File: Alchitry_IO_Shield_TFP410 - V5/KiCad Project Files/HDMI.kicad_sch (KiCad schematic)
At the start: 19 parts, among them J1 HDMI_A_1.4, U2 TFP410

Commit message: started new shield
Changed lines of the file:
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@@
-(kicad_sch (version 20200714) (host eeschema "(5.99.0-2416-g010316457)")
-  (page 1 3)
+(kicad_sch (version 20200714) (host eeschema "(5.99.0-2671-gfc0a358ba)")
+  (page 2 3)
   (paper "A4")
-  (junction (at 95.25 67.945) (diameter 0) (color 0 0 0 0))
-  (junction (at 95.25 69.215) (diameter 0) (color 0 0 0 0))
-  (junction (at 95.25 70.485) (diameter 0) (color 0 0 0 0))
-  (junction (at 95.25 88.265) (diameter 0) (color 0 0 0 0))
-  (junction (at 95.25 89.535) (diameter 0) (color 0 0 0 0))
-  (junction (at 95.25 90.805) (diameter 0) (color 0 0 0 0))
-  (junction (at 95.25 108.585) (diameter 0) (color 0 0 0 0))
-  (junction (at 95.25 109.855) (diameter 0) (color 0 0 0 0))
-  (junction (at 95.25 111.125) (diameter 0) (color 0 0 0 0))
-  (junction (at 98.425 135.89) (diameter 0) (color 0 0 0 0))
-  (junction (at 107.315 135.89) (diameter 0) (color 0 0 0 0))
-  (junction (at 113.03 148.59) (diameter 0) (color 0 0 0 0))
-  (junction (at 115.57 137.795) (diameter 0) (color 0 0 0 0))
-  (junction (at 115.57 148.59) (diameter 0) (color 0 0 0 0))
-  (junction (at 118.11 148.59) (diameter 0) (color 0 0 0 0))
-  (junction (at 147.955 90.17) (diameter 0) (color 0 0 0 0))
-  (junction (at 147.955 92.71) (diameter 0) (color 0 0 0 0))
-  (junction (at 147.955 95.25) (diameter 0) (color 0 0 0 0))
-  (junction (at 147.955 97.79) (diameter 0) (color 0 0 0 0))
-  (junction (at 147.955 100.33) (diameter 0) (color 0 0 0 0))
-  (junction (at 147.955 102.87) (diameter 0) (color 0 0 0 0))
-  (junction (at 147.955 105.41) (diameter 0) (color 0 0 0 0))
-  (junction (at 147.955 107.95) (diameter 0) (color 0 0 0 0))
-  (junction (at 151.765 67.945) (diameter 0) (color 0 0 0 0))
-  (junction (at 151.765 69.215) (diameter 0) (color 0 0 0 0))
-  (junction (at 151.765 74.93) (diameter 0) (color 0 0 0 0))
-  (junction (at 151.765 75.565) (diameter 0) (color 0 0 0 0))
-  (junction (at 151.765 81.915) (diameter 0) (color 0 0 0 0))
-  (junction (at 156.845 68.58) (diameter 0) (color 0 0 0 0))
-  (junction (at 156.845 69.215) (diameter 0) (color 0 0 0 0))
-  (junction (at 156.845 74.295) (diameter 0) (color 0 0 0 0))
-  (junction (at 156.845 75.565) (diameter 0) (color 0 0 0 0))
-  (junction (at 156.845 80.645) (diameter 0) (color 0 0 0 0))
-  (junction (at 159.385 60.325) (diameter 0) (color 0 0 0 0))
-  (junction (at 161.925 69.215) (diameter 0) (color 0 0 0 0))
-  (junction (at 161.925 74.295) (diameter 0) (color 0 0 0 0))
-  (junction (at 164.465 60.325) (diameter 0) (color 0 0 0 0))
-  (junction (at 164.465 67.31) (diameter 0) (color 0 0 0 0))
-  (junction (at 167.005 80.645) (diameter 0) (color 0 0 0 0))
-  (junction (at 167.005 86.995) (diameter 0) (color 0 0 0 0))
-  (junction (at 170.815 60.325) (diameter 0) (color 0 0 0 0))
-  (junction (at 174.625 60.325) (diameter 0) (color 0 0 0 0))
-  (junction (at 193.04 45.72) (diameter 0) (color 0 0 0 0))
-  (junction (at 196.215 108.585) (diameter 0) (color 0 0 0 0))
-  (junction (at 198.755 50.165) (diameter 0) (color 0 0 0 0))
-  (junction (at 198.755 108.585) (diameter 0) (color 0 0 0 0))
-  (junction (at 200.025 108.585) (diameter 0) (color 0 0 0 0))
-  (junction (at 201.295 108.585) (diameter 0) (color 0 0 0 0))
-  (junction (at 203.835 108.585) (diameter 0) (color 0 0 0 0))
-  (no_connect (at 188.595 86.36))
-  (no_connect (at 188.595 88.9))
-  (no_connect (at 188.595 93.98))
-  (no_connect (at 188.595 96.52))
+  (junction (at 95.25 67.945) (diameter 1.016) (color 0 0 0 0))
+  (junction (at 95.25 69.215) (diameter 1.016) (color 0 0 0 0))
+  (junction (at 95.25 70.485) (diameter 1.016) (color 0 0 0 0))
+  (junction (at 95.25 88.265) (diameter 1.016) (color 0 0 0 0))
+  (junction (at 95.25 89.535) (diameter 1.016) (color 0 0 0 0))
+  (junction (at 95.25 90.805) (diameter 1.016) (color 0 0 0 0))
+  (junction (at 95.25 108.585) (diameter 1.016) (color 0 0 0 0))
+  (junction (at 95.25 109.855) (diameter 1.016) (color 0 0 0 0))
+  (junction (at 95.25 111.125) (diameter 1.016) (color 0 0 0 0))
+  (junction (at 98.425 135.89) (diameter 1.016) (color 0 0 0 0))
+  (junction (at 107.315 135.89) (diameter 1.016) (color 0 0 0 0))
+  (junction (at 113.03 148.59) (diameter 1.016) (color 0 0 0 0))
+  (junction (at 115.57 137.795) (diameter 1.016) (color 0 0 0 0))
+  (junction (at 115.57 148.59) (diameter 1.016) (color 0 0 0 0))
+  (junction (at 118.11 148.59) (diameter 1.016) (color 0 0 0 0))
+  (junction (at 147.955 90.17) (diameter 1.016) (color 0 0 0 0))
+  (junction (at 147.955 92.71) (diameter 1.016) (color 0 0 0 0))
+  (junction (at 147.955 95.25) (diameter 1.016) (color 0 0 0 0))
+  (junction (at 147.955 97.79) (diameter 1.016) (color 0 0 0 0))
+  (junction (at 147.955 100.33) (diameter 1.016) (color 0 0 0 0))
+  (junction (at 147.955 102.87) (diameter 1.016) (color 0 0 0 0))
+  (junction (at 147.955 105.41) (diameter 1.016) (color 0 0 0 0))
+  (junction (at 147.955 107.95) (diameter 1.016) (color 0 0 0 0))
+  (junction (at 151.765 67.945) (diameter 1.016) (color 0 0 0 0))
+  (junction (at 151.765 69.215) (diameter 1.016) (color 0 0 0 0))
+  (junction (at 151.765 74.93) (diameter 1.016) (color 0 0 0 0))
+  (junction (at 151.765 75.565) (diameter 1.016) (color 0 0 0 0))
+  (junction (at 151.765 81.915) (diameter 1.016) (color 0 0 0 0))
+  (junction (at 156.845 68.58) (diameter 1.016) (color 0 0 0 0))
+  (junction (at 156.845 69.215) (diameter 1.016) (color 0 0 0 0))
+  (junction (at 156.845 74.295) (diameter 1.016) (color 0 0 0 0))
+  (junction (at 156.845 75.565) (diameter 1.016) (color 0 0 0 0))
+  (junction (at 156.845 80.645) (diameter 1.016) (color 0 0 0 0))
+  (junction (at 159.385 60.325) (diameter 1.016) (color 0 0 0 0))
+  (junction (at 161.925 69.215) (diameter 1.016) (color 0 0 0 0))
+  (junction (at 161.925 74.295) (diameter 1.016) (color 0 0 0 0))
+  (junction (at 164.465 60.325) (diameter 1.016) (color 0 0 0 0))
+  (junction (at 164.465 67.31) (diameter 1.016) (color 0 0 0 0))
+  (junction (at 167.005 80.645) (diameter 1.016) (color 0 0 0 0))
+  (junction (at 167.005 86.995) (diameter 1.016) (color 0 0 0 0))
+  (junction (at 170.815 60.325) (diameter 1.016) (color 0 0 0 0))
+  (junction (at 174.625 60.325) (diameter 1.016) (color 0 0 0 0))
+  (junction (at 193.04 45.72) (diameter 1.016) (color 0 0 0 0))
+  (junction (at 196.215 108.585) (diameter 1.016) (color 0 0 0 0))
+  (junction (at 198.755 50.165) (diameter 1.016) (color 0 0 0 0))
+  (junction (at 198.755 108.585) (diameter 1.016) (color 0 0 0 0))
+  (junction (at 200.025 108.585) (diameter 1.016) (color 0 0 0 0))
+  (junction (at 201.295 108.585) (diameter 1.016) (color 0 0 0 0))
+  (junction (at 203.835 108.585) (diameter 1.016) (color 0 0 0 0))
   (no_connect (at 139.065 129.54))
   (no_connect (at 188.595 81.28))
+  (no_connect (at 188.595 88.9))
+  (no_connect (at 188.595 96.52))
+  (no_connect (at 188.595 93.98))
+  (no_connect (at 188.595 86.36))
   (bus_entry (at 88.9 52.705) (size 2.54 2.54)
     (stroke (width 0.1524) (type solid) (color 0 0 0 0))
@@
     (stroke (width 0) (type solid) (color 0 0 0 0))
   )
-  (bus (pts (xy 88.9 52.705) (xy 88.9 57.785))
+  (bus (pts (xy 88.9 52.705) (xy 88.9 55.245))
+    (stroke (width 0) (type solid) (color 0 0 0 0))
+  )
+  (bus (pts (xy 88.9 55.245) (xy 88.9 57.785))
     (stroke (width 0) (type solid) (color 0 0 0 0))
   )
@@
     (stroke (width 0) (type solid) (color 0 0 0 0))
   )
-  (bus (pts (xy 88.9 75.565) (xy 88.9 80.645))
+  (bus (pts (xy 88.9 75.565) (xy 88.9 78.105))
+    (stroke (width 0) (type solid) (color 0 0 0 0))
+  )
+  (bus (pts (xy 88.9 78.105) (xy 88.9 80.645))
     (stroke (width 0) (type solid) (color 0 0 0 0))
   )
@@
     (stroke (width 0) (type solid) (color 0 0 0 0))
   )
-  (bus (pts (xy 88.9 93.345) (xy 88.9 98.425))
-    (stroke (width 0) (type solid) (color 0 0 0 0))
-  )
+  (bus (pts (xy 88.9 93.345) (xy 88.9 95.885))
+    (stroke (width 0) (type solid) (color 0 0 0 0))
+  )
+  (bus (pts (xy 88.9 95.885) (xy 88.9 98.425))
+    (stroke (width 0) (type solid) (color 0 0 0 0))
+  )

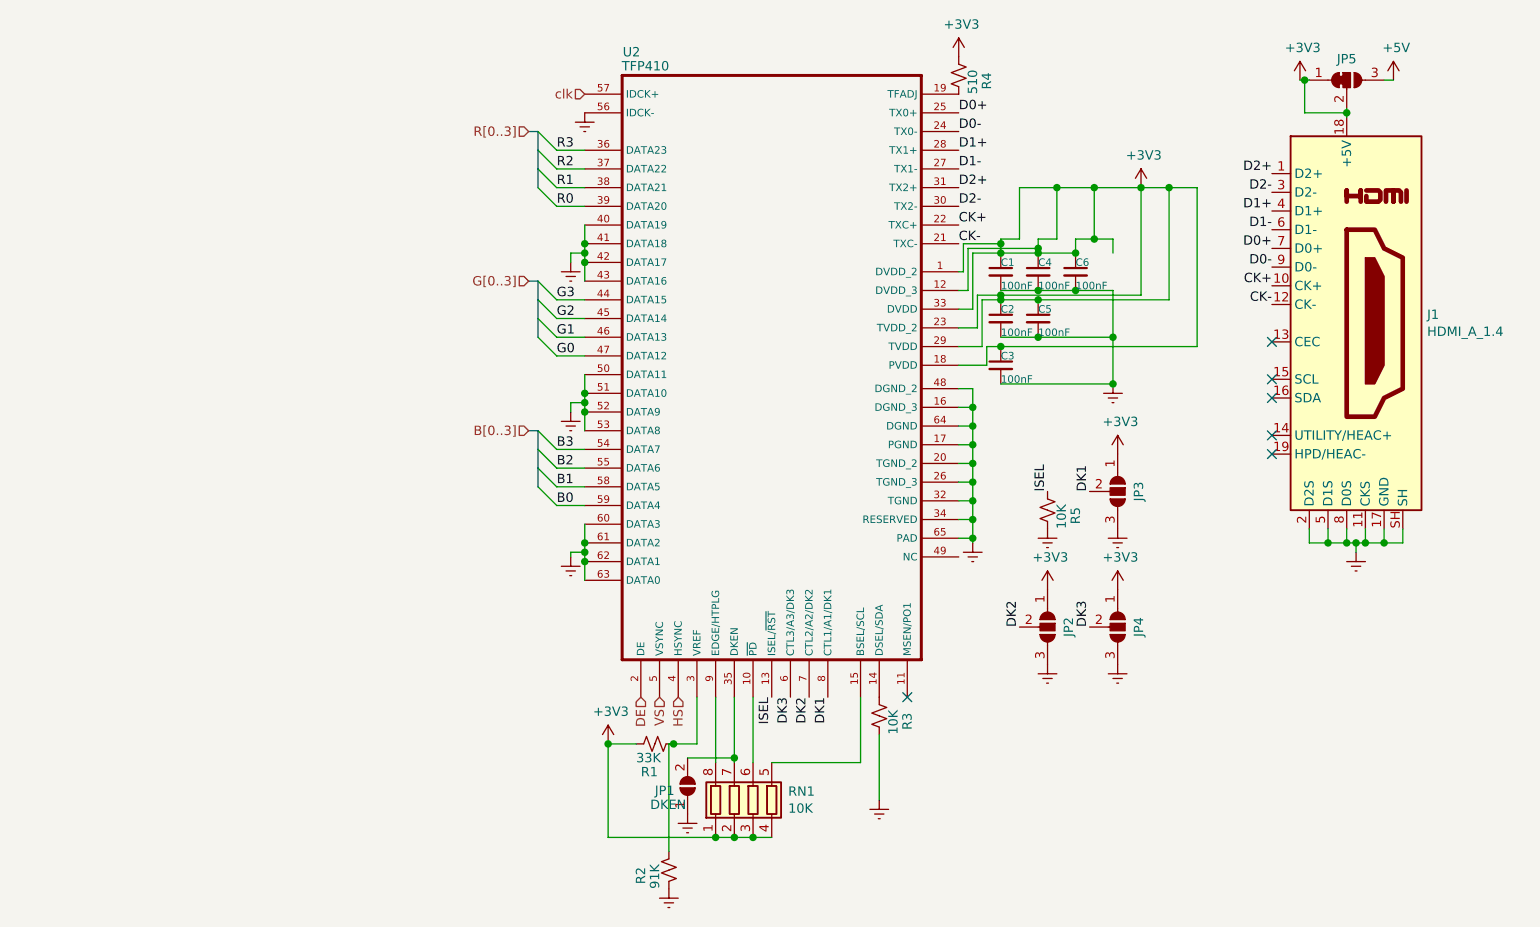
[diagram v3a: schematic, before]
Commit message: adding USB C for OTG programming and serial
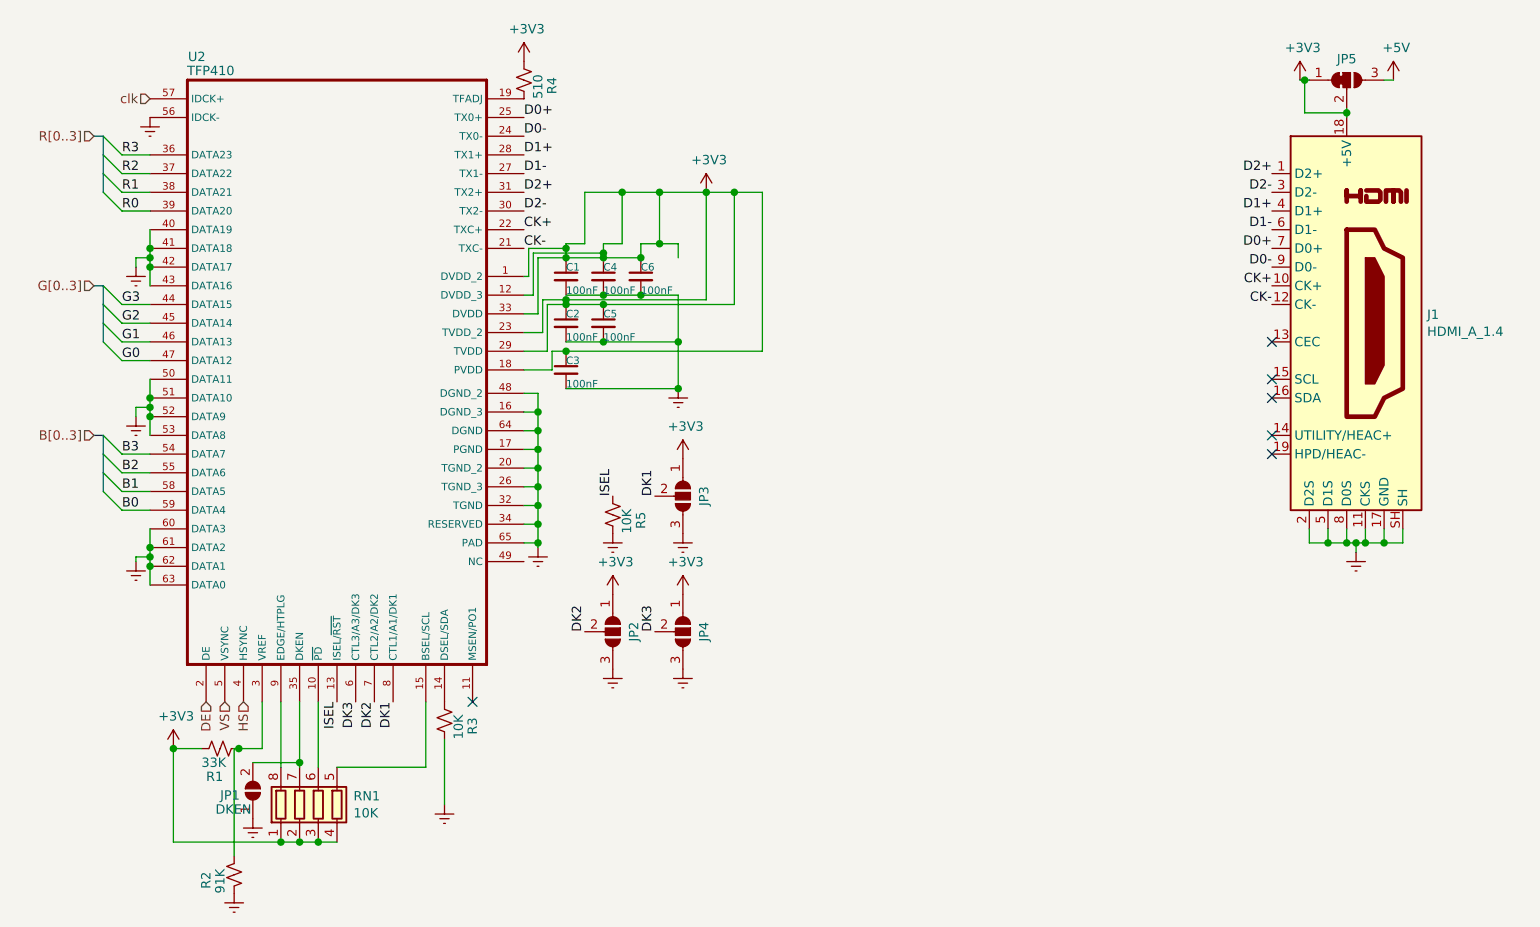
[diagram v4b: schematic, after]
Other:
- moved on the sheet: C1, C2, C3, C4, C5, C6, JP1, JP2, JP3, JP4, R1, R2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
